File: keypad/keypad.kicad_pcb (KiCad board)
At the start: 2 copper layers, 50 x 58.2 mm, 60 parts, among them J1 NO FIT, P1 GT-USB-7010ASV, Q1 BC807-40LT1G, SW1 TS04-66-70-BK-100-SMT, SW2 TS04-66-70-BK-100-SMT, SW3 NO FIT, SW4 NO FIT, SW5 NO FIT, U1 RP2040, U3 W25Q16JVSSIQ, U4 NCP1117-3.3_SOT223, U5 DRV5053VAQDBZR, U6 DRV5053VAQDBZR, Y1 NX3225SA-12MHz-STD-CSR-6

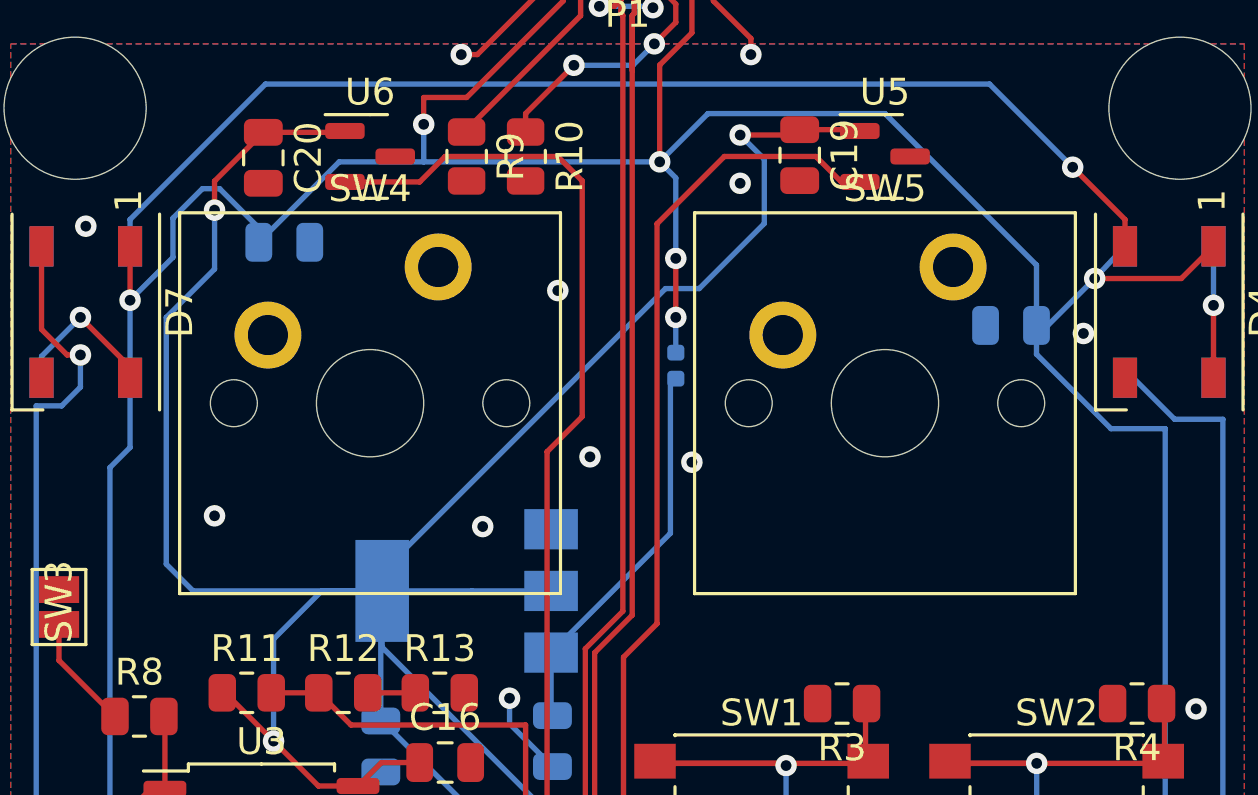
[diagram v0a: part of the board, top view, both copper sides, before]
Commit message: move switches slighltly
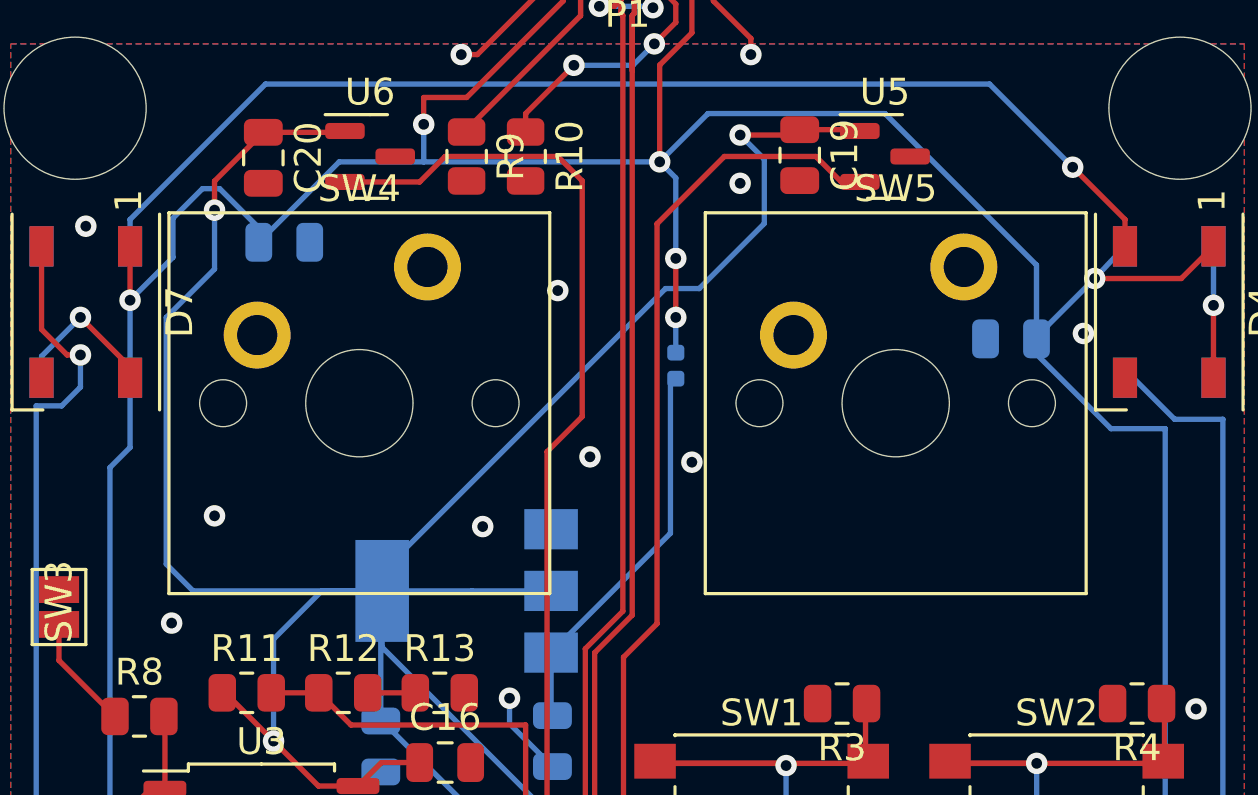
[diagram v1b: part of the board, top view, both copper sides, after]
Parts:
- moved C15 0.50 mm to (119.3, 77.0)
- moved SW4 0.40 mm to (95.0, 79.4)
- moved SW5 0.40 mm to (115.0, 79.4)
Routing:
- net VBUS: track 154.1 -> 155.9 mm
- net GND: vias 25 -> 26
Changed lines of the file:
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@@
   (net 69 "Net-(Q1-Pad1)")
   (footprint "Switch_Keyboard_Cherry_MX:SW_Cherry_MX_PCB_1.00u" (layer "F.Cu")
-    (at 95.4 79.4)
+    (at 95 79.4)
     (descr "Cherry MX keyswitch PCB Mount with 1.00u keycap")
     (tags "Cherry MX Keyboard Keyswitch Switch PCB Cutout 1.00u")
@@
   )
   (footprint "Switch_Keyboard_Cherry_MX:SW_Cherry_MX_PCB_1.00u" (layer "F.Cu")
-    (at 114.6 79.4)
+    (at 115 79.4)
     (descr "Cherry MX keyswitch PCB Mount with 1.00u keycap")
     (tags "Cherry MX Keyboard Keyswitch Switch PCB Cutout 1.00u")
@@
   )
   (footprint "Capacitor_SMD:C_0805_2012Metric" (layer "B.Cu")
-    (at 119.3 76.5 180)
+    (at 119.3 77 180)
     (descr "Capacitor SMD 0805 (2012 Metric), square (rectangular) end terminal, IPC_7351 nominal, (Body size source: IPC-SM-782 page 76, https://www.pcb-3d.com/wordpress/wp-content/uploads/ipc-sm-782a_amendment_1_and_2.pdf, https://docs.google.com/spreadsheets/d/1BsfQQcO9C6DZCsRaXUlFlo91Tg2WpOkGARC1WS5S8t0/edit?usp=sharing), generated with kicad-footprint-generator")
     (tags "capacitor")
@@
   (via (at 114.4 105.6) (size 0.8) (drill 0.4) (layers "F.Cu" "B.Cu") (free) (net 2))
   (via (at 91.4 95.4) (size 0.8) (drill 0.4) (layers "F.Cu" "B.Cu") (net 2))
+  (via (at 88 87.6) (size 0.8) (drill 0.4) (layers "F.Cu" "B.Cu") (free) (net 2))
   (via (at 100.6 90.4) (size 0.8) (drill 0.4) (layers "F.Cu" "B.Cu") (free) (net 2))
   (via (at 102.4 75.2) (size 0.8) (drill 0.4) (layers "F.Cu" "B.Cu") (free) (net 2))
@@
   (segment (start 97.4 70.4) (end 106.2 70.4) (width 0.2) (layer "B.Cu") (net 8))
   (segment (start 120.25 76.5) (end 120.670853 76.5) (width 0.2) (layer "B.Cu") (net 8))
-  (segment (start 120.25 74.25) (end 120.25 76.5) (width 0.2) (layer "B.Cu") (net 8))
+  (segment (start 120.25 74.25) (end 120.25 77) (width 0.2) (layer "B.Cu") (net 8))
   (segment (start 87.85 100.95) (end 85.75 100.95) (width 0.2) (layer "B.Cu") (net 8))
   (segment (start 117.4625 108.05) (end 119.6 105.9125) (width 0.2) (layer "B.Cu") (net 8))
@@
   (segment (start 89.78995 71.4) (end 89.15 71.4) (width 0.2) (layer "B.Cu") (net 8))
   (segment (start 85.75 100.95) (end 85.7 100.9) (width 0.2) (layer "B.Cu") (net 8))
-  (segment (start 120.25 77.573652) (end 123.026348 80.35) (width 0.2) (layer "B.Cu") (net 8))
   (segment (start 89.15 71.4) (end 88.05 72.5) (width 0.2) (layer "B.Cu") (net 8))
   (segment (start 85.7 81.8) (end 86.45 81.05) (width 0.2) (layer "B.Cu") (net 8))
   (segment (start 120.9 104.05) (end 119.6 105.35) (width 0.2) (layer "B.Cu") (net 8))
   (segment (start 121.95 104.05) (end 122.15 104.05) (width 0.2) (layer "B.Cu") (net 8))
+  (segment (start 120.25 77.573652) (end 123.026348 80.35) (width 0.2) (layer "B.Cu") (net 8))
   (segment (start 121.95 104.05) (end 120.9 104.05) (width 0.2) (layer "B.Cu") (net 8))
+  (segment (start 120.25 76.920853) (end 122.420102 74.750751) (width 0.2) (layer "B.Cu") (net 8))
   (segment (start 88.05 72.5) (end 88.05 73.96005) (width 0.2) (layer "B.Cu") (net 8))
   (segment (start 94.25 70.4) (end 91.25 73.4) (width 0.2) (layer "B.Cu") (net 8))
@@
   (segment (start 120.25 76.5) (end 120.25 77.573652) (width 0.2) (layer "B.Cu") (net 8))
   (segment (start 119.6 105.9125) (end 119.6 105.35) (width 0.2) (layer "B.Cu") (net 8))
+  (segment (start 120.25 77) (end 120.25 77.573652) (width 0.2) (layer "B.Cu") (net 8))
   (segment (start 86.45 81.05) (end 86.45 78.45) (width 0.2) (layer "B.Cu") (net 8))
   (segment (start 106.8 77.515) (end 106.8 76.2) (width 0.2) (layer "B.Cu") (net 8))
@@
   (segment (start 85.7 100.9) (end 85.7 81.8) (width 0.2) (layer "B.Cu") (net 8))
   (segment (start 91.25 73.4) (end 91.25 72.86005) (width 0.2) (layer "B.Cu") (net 8))
-  (segment (start 120.670853 76.5) (end 122.420102 74.750751) (width 0.2) (layer "B.Cu") (net 8))
+  (segment (start 120.25 77) (end 120.25 76.920853) (width 0.2) (layer "B.Cu") (net 8))
   (segment (start 125.05 80.35) (end 125.05 101.15) (width 0.2) (layer "B.Cu") (net 8))
   (segment (start 106.6 84.25) (end 106.6 78.685) (width 0.2) (layer "B.Cu") (net 9))
@@
     (connect_pads (clearance 0.508))
     (min_thickness 0.254) (filled_areas_thickness no)
-    (fill (thermal_gap 0.508) (thermal_bridge_width 0.508))
+    (fill yes (thermal_gap 0.508) (thermal_bridge_width 0.508))
     (polygon
       (pts
@@
     (connect_pads (clearance 0.508))
     (min_thickness 0.254) (filled_areas_thickness no)
-    (fill (thermal_gap 0.508) (thermal_bridge_width 0.508))
+    (fill yes (thermal_gap 0.508) (thermal_bridge_width 0.508))
     (polygon
       (pts

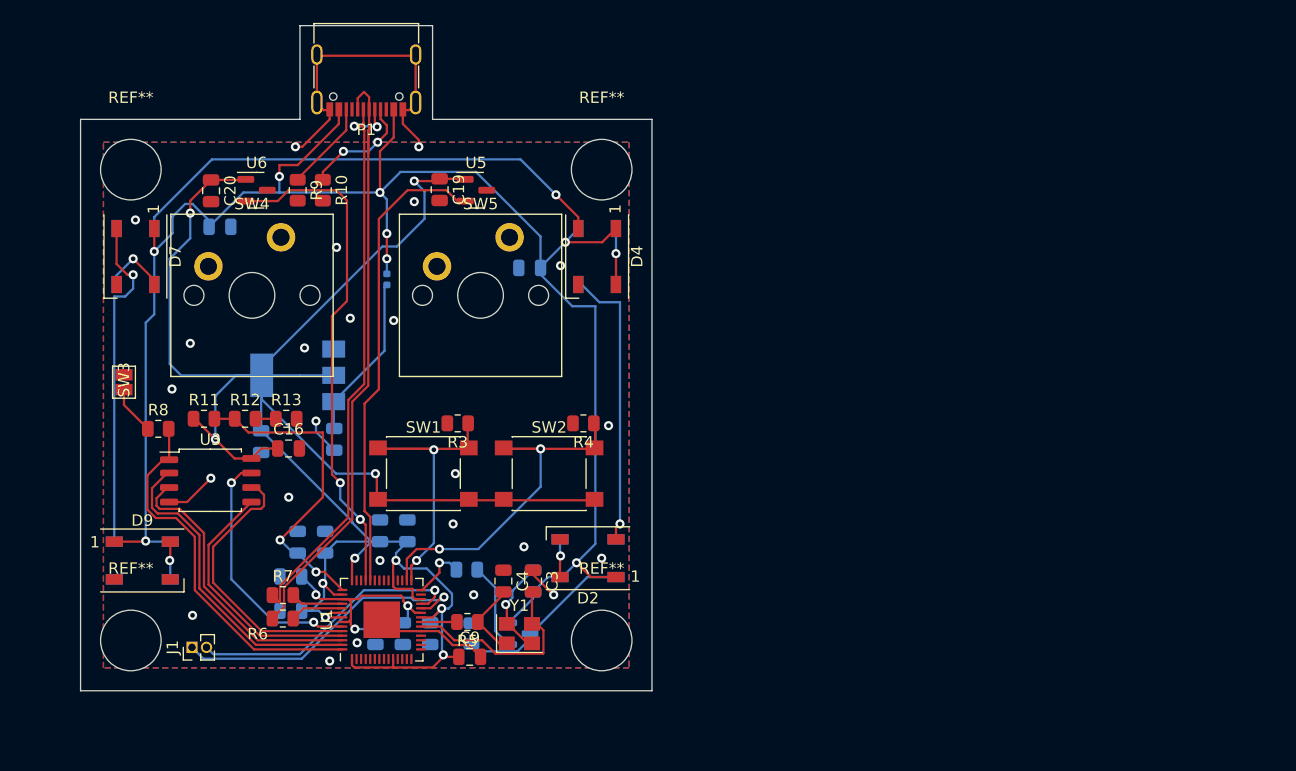
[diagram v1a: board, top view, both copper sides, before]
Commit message: Size increase to accomodate for mechanical
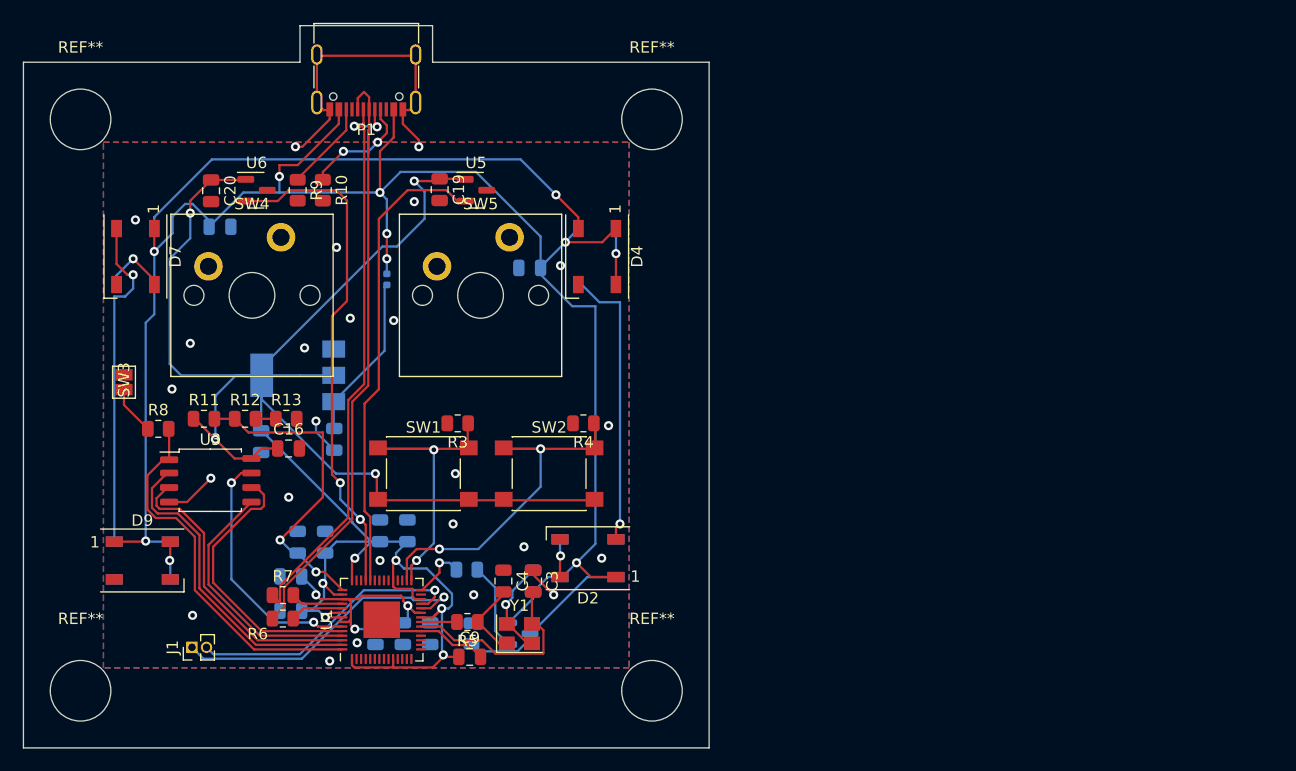
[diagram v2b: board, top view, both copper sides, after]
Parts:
- moved REF** 6.22 mm to (80.0, 114.0)
- moved REF** 6.22 mm to (80.0, 64.0)
- moved REF** 6.22 mm to (130.0, 114.0)
- moved REF** 6.22 mm to (130.0, 64.0)
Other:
- board size 50 x 58.2 mm -> 60 x 63.2 mm
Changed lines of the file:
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@@
   )
   (footprint "MountingHole:MountingHole_5.3mm_M5" (layer "F.Cu")
-    (at 84.4 109.6)
+    (at 80 114)
     (descr "Mounting Hole 5.3mm, no annular, M5")
     (tags "mounting hole 5.3mm no annular m5")
@@
   )
   (footprint "MountingHole:MountingHole_5.3mm_M5" (layer "F.Cu")
-    (at 84.4 68.4)
+    (at 80 64)
     (descr "Mounting Hole 5.3mm, no annular, M5")
     (tags "mounting hole 5.3mm no annular m5")
@@
   )
   (footprint "MountingHole:MountingHole_5.3mm_M5" (layer "F.Cu")
-    (at 125.6 109.6)
+    (at 130 114)
     (descr "Mounting Hole 5.3mm, no annular, M5")
     (tags "mounting hole 5.3mm no annular m5")
@@
   )
   (footprint "MountingHole:MountingHole_5.3mm_M5" (layer "F.Cu")
-    (at 125.6 68.4)
+    (at 130 64)
     (descr "Mounting Hole 5.3mm, no annular, M5")
     (tags "mounting hole 5.3mm no annular m5")
@@
     )
   )
-  (gr_circle (center 125.6 109.6) (end 128.6 109.6) (layer "Dwgs.User") (width 0.1) (fill none))
-  (gr_circle (center 125.6 68.4) (end 128.6 68.4) (layer "Dwgs.User") (width 0.1) (fill none))
-  (gr_circle (center 84.4 68.4) (end 87.4 68.4) (layer "Dwgs.User") (width 0.1) (fill none))
-  (gr_circle (center 84.4 109.6) (end 87.4 109.6) (layer "Dwgs.User") (width 0.1) (fill none))
   (gr_poly locked
     (pts
-      (xy 110.8 64)
-      (xy 130 64)
-      (xy 130 114)
-      (xy 80 114)
-      (xy 80 64)
-      (xy 99.2 64)
+      (xy 110.8 59)
+      (xy 135 59)
+      (xy 135 119)
+      (xy 75 119)
+      (xy 75 59)
+      (xy 99.2 59)
       (xy 99.2 55.8)
       (xy 110.8 55.8)
@@
     (connect_pads (clearance 0.508))
     (min_thickness 0.254) (filled_areas_thickness no)
-    (fill yes (thermal_gap 0.508) (thermal_bridge_width 0.508))
+    (fill (thermal_gap 0.508) (thermal_bridge_width 0.508))
     (polygon
       (pts
@@
     (connect_pads (clearance 0.508))
     (min_thickness 0.254) (filled_areas_thickness no)
-    (fill yes (thermal_gap 0.508) (thermal_bridge_width 0.508))
+    (fill (thermal_gap 0.508) (thermal_bridge_width 0.508))
     (polygon
       (pts

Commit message: fix up stuff for fab
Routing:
- net USB_DP: track 53.6 -> 51.6 mm
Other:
- board text added: "JLCJLCJLCJLC"
- board text added: "rev2 - prototype model"
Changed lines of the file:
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@@
       (layerselection 0x00010fc_ffffffff)
       (disableapertmacros false)
-      (usegerberextensions false)
+      (usegerberextensions true)
       (usegerberattributes true)
       (usegerberadvancedattributes true)
@@
       (plotinvisibletext false)
       (sketchpadsonfab false)
-      (subtractmaskfromsilk false)
+      (subtractmaskfromsilk true)
       (outputformat 1)
       (mirror false)
@@
       (xy 110.8 55.8)
     ) (layer "Edge.Cuts") (width 0.1) (fill none))
+  (gr_text "JLCJLCJLCJLC" (at 115.55 83.8) (layer "B.SilkS")
+    (effects (font (size 1 1) (thickness 0.15)) (justify mirror))
+  )
+  (gr_text "rev2 - prototype model\n" (at 115.55 86.25) (layer "B.SilkS")
+    (effects (font (size 1 1) (thickness 0.15)) (justify mirror))
+  )
   (segment (start 110.83 92.83) (end 105.925 92.83) (width 0.2) (layer "F.Cu") (net 1))
   (segment (start 110.9125 92.9125) (end 110.83 92.83) (width 0.2) (layer "F.Cu") (net 1))
@@
   (segment (start 120.45 110.75) (end 120.5 110.7) (width 0.2) (layer "F.Cu") (net 4))
   (segment (start 111.5 108.38) (end 112.7 109.58) (width 0.2) (layer "F.Cu") (net 4))
-  (segment (start 119.6 105.35) (end 119.8 105.55) (width 0.2) (layer "F.Cu") (net 4))
   (segment (start 112.7 109.58) (end 115.13 109.58) (width 0.2) (layer "F.Cu") (net 4))
   (segment (start 120.5 110.7) (end 120.5 108.7) (width 0.2) (layer "F.Cu") (net 4))
   (segment (start 117.3 109.85) (end 116.6325 109.85) (width 0.2) (layer "F.Cu") (net 5))
-  (segment (start 117.15 105.35) (end 117 105.35) (width 0.2) (layer "F.Cu") (net 5))
-  (segment (start 117 105.48) (end 117 105.35) (width 0.2) (layer "F.Cu") (net 5))
+  (segment (start 114.7625 107.5875) (end 117 105.35) (width 0.2) (layer "F.Cu") (net 5))
   (segment (start 116.6325 109.85) (end 114.7625 107.98) (width 0.2) (layer "F.Cu") (net 5))
-  (segment (start 114.7625 107.98) (end 114.7625 107.80875) (width 0.2) (layer "F.Cu") (net 5))
-  (segment (start 117 105.57125) (end 117 105.48) (width 0.2) (layer "F.Cu") (net 5))
-  (segment (start 114.7625 107.80875) (end 117 105.57125) (width 0.2) (layer "F.Cu") (net 5))
+  (segment (start 114.7625 107.98) (end 114.7625 107.5875) (width 0.2) (layer "F.Cu") (net 5))
   (segment (start 109.255025 107.18) (end 109.7875 107.18) (width 0.2) (layer "F.Cu") (net 6))
   (segment (start 103.444975 107.98) (end 103.65 107.774975) (width 0.2) (layer "F.Cu") (net 6))
@@
   (segment (start 111.42 69.2) (end 113.6125 69.2) (width 0.2) (layer "F.Cu") (net 7))
   (segment (start 110.82 107.58) (end 111.6 106.8) (width 0.2) (layer "F.Cu") (net 7))
-  (segment (start 109.2 69.4) (end 109.4 69.2) (width 0.2) (layer "F.Cu") (net 7))
   (segment (start 107.555025 105.08) (end 107.35 104.874975) (width 0.2) (layer "F.Cu") (net 7))
   (segment (start 89.6 71.12) (end 91.42 69.3) (width 0.2) (layer "F.Cu") (net 7))
@@
   (segment (start 97.05 92.8) (end 95.825 92.8) (width 0.2) (layer "F.Cu") (net 7))
   (segment (start 103.955025 111.955) (end 103.75 111.749975) (width 0.2) (layer "F.Cu") (net 7))
-  (segment (start 91.42 69.3) (end 91.47 69.25) (width 0.2) (layer "F.Cu") (net 7))
   (segment (start 105.925 95.125) (end 105.8 95) (width 0.2) (layer "F.Cu") (net 7))
   (segment (start 105.925 97.33) (end 113.875 97.33) (width 0.2) (layer "F.Cu") (net 7))
@@
   (segment (start 126.85 78.45) (end 126.85 75.75) (width 0.2) (layer "F.Cu") (net 13))
   (via (at 126.85 75.75) (size 0.8) (drill 0.4) (layers "F.Cu" "B.Cu") (net 13))
-  (segment (start 126.85 75.75) (end 126.8 75.8) (width 0.2) (layer "B.Cu") (net 13))
   (segment (start 126.85 73.55) (end 126.85 75.75) (width 0.2) (layer "B.Cu") (net 13))
   (segment (start 123.55 73.55) (end 123.55 72.55) (width 0.2) (layer "F.Cu") (net 14))
@@
   (segment (start 83.15 77.65) (end 84.6 76.2) (width 0.2) (layer "B.Cu") (net 15))
   (segment (start 101.2 68.6) (end 103 66.8) (width 0.2) (layer "F.Cu") (net 16))
-  (segment (start 105.8 65.8) (end 106 66) (width 0.2) (layer "F.Cu") (net 16))
   (segment (start 106.25 63.965) (end 106.8 64.515) (width 0.2) (layer "F.Cu") (net 16))
   (segment (start 106.8 65.2) (end 106 66) (width 0.2) (layer "F.Cu") (net 16))
@@
   (segment (start 104.8 61.6) (end 105.25 62.05) (width 0.2) (layer "F.Cu") (net 17))
   (segment (start 105.175 64.942501) (end 105.25 64.867501) (width 0.2) (layer "F.Cu") (net 17))
-  (segment (start 105.175 67) (end 105.175 64.942501) (width 0.2) (layer "F.Cu") (net 17))
   (segment (start 104.25 63.19) (end 104.25 62.15) (width 0.2) (layer "F.Cu") (net 17))
   (segment (start 103.775 88.702488) (end 105.175 87.302488) (width 0.2) (layer "F.Cu") (net 17))
@@
     (connect_pads (clearance 0.508))
     (min_thickness 0.254) (filled_areas_thickness no)
-    (fill (thermal_gap 0.508) (thermal_bridge_width 0.508))
+    (fill yes (thermal_gap 0.508) (thermal_bridge_width 0.508))
     (polygon
       (pts
@@
     (connect_pads (clearance 0.508))
     (min_thickness 0.254) (filled_areas_thickness no)
-    (fill (thermal_gap 0.508) (thermal_bridge_width 0.508))
+    (fill yes (thermal_gap 0.508) (thermal_bridge_width 0.508))
     (polygon
       (pts
